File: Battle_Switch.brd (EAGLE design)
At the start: 160 x 100 mm, 10 parts, among them IC1 ATTINY13A

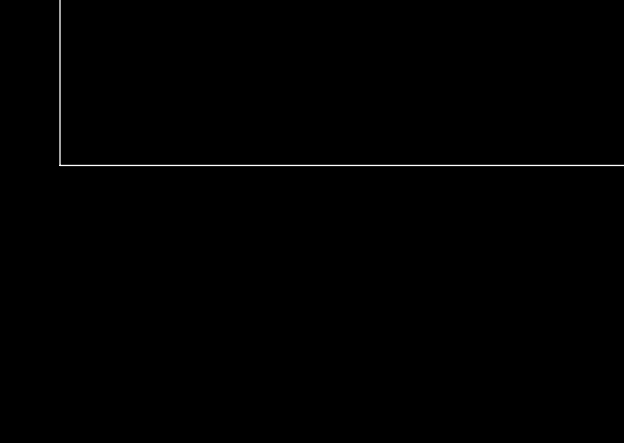
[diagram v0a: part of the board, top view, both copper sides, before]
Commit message: Added mode and threshold select jumpers.
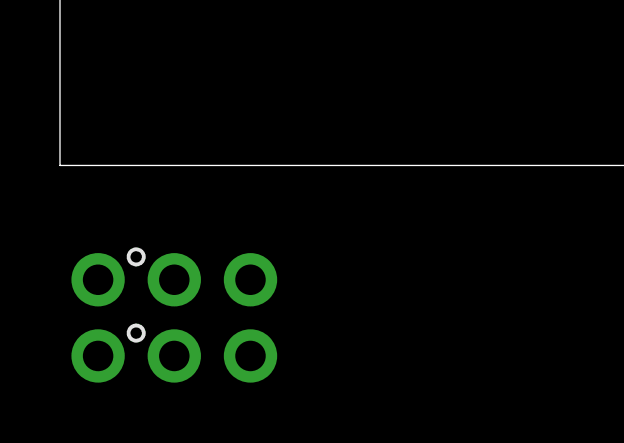
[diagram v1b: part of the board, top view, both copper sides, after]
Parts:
- added SJ1, SJ2: JUMPER-PTH-3-2OF3_NC, Battle_Switch:PTH-JUMPER-3-20F3_NC
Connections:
- new net THRESH_SEL: SJ2.P$1
- net GND: now also SJ1.P$2, SJ2.P$2
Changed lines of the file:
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@@
 <layer number="49" name="Reference" color="7" fill="1" visible="yes" active="yes"/>
 <layer number="50" name="dxf" color="7" fill="1" visible="no" active="no"/>
-<layer number="51" name="tDocu" color="7" fill="1" visible="no" active="yes"/>
+<layer number="51" name="tDocu" color="7" fill="1" visible="yes" active="yes"/>
 <layer number="52" name="bDocu" color="7" fill="1" visible="no" active="yes"/>
 <layer number="53" name="tGND_GNDA" color="7" fill="9" visible="no" active="no"/>
@@
 <element name="R1" library="Battle_Switch" package="0411/15" value="10k" x="25.4" y="60.96" rot="R180"/>
 <element name="R2" library="Battle_Switch" package="0411/15" value="10k" x="43.18" y="60.96" rot="R180"/>
+<element name="SJ2" library="Battle_Switch" package="PTH-JUMPER-3-20F3_NC" value="JUMPER-PTH-3-2OF3_NC" x="3.81" y="-3.81"/>
+<element name="SJ1" library="Battle_Switch" package="PTH-JUMPER-3-20F3_NC" value="JUMPER-PTH-3-2OF3_NC" x="3.81" y="-6.35"/>
 </elements>
 <signals>
@@
 <wire x1="54.61" y1="62.23" x2="54.61" y2="50.8" width="1.778" layer="16"/>
 <wire x1="41.91" y1="50.8" x2="54.61" y2="50.8" width="1.778" layer="16"/>
+<contactref element="SJ1" pad="P$2"/>
+<contactref element="SJ2" pad="P$2"/>
+<wire x1="3.81" y1="-3.81" x2="17.78" y2="60.96" width="0" layer="19" extent="1-1"/>
+<wire x1="3.81" y1="-6.35" x2="3.81" y2="-3.81" width="0" layer="19" extent="1-1"/>
 </signal>
 <signal name="VIN">
@@
 <contactref element="IC1" pad="P$7"/>
 </signal>
+<signal name="THRESH_SEL">
+<contactref element="SJ2" pad="P$1"/>
+</signal>
 </signals>

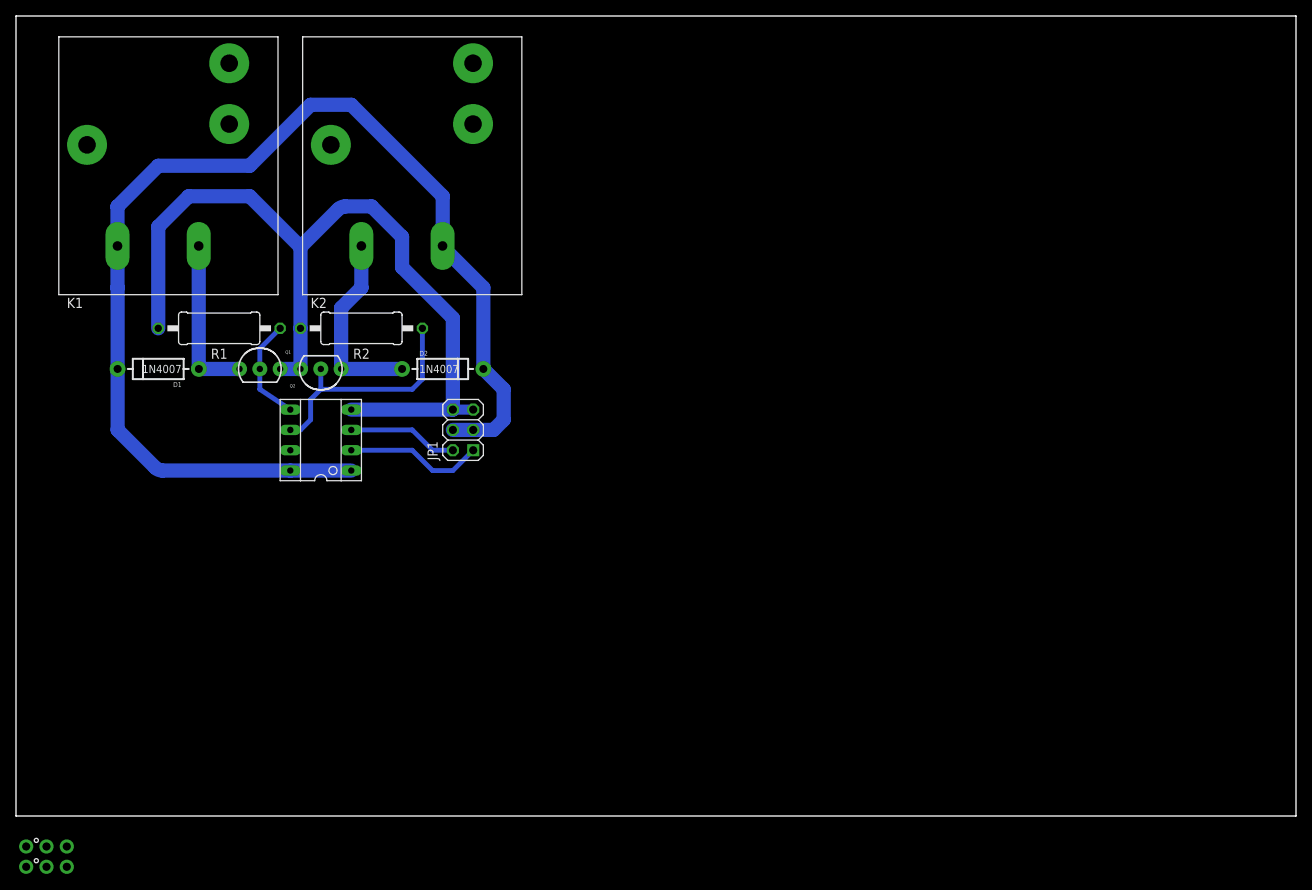
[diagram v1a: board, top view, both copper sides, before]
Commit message: Completed board layout.  Ready for copper ground pour.
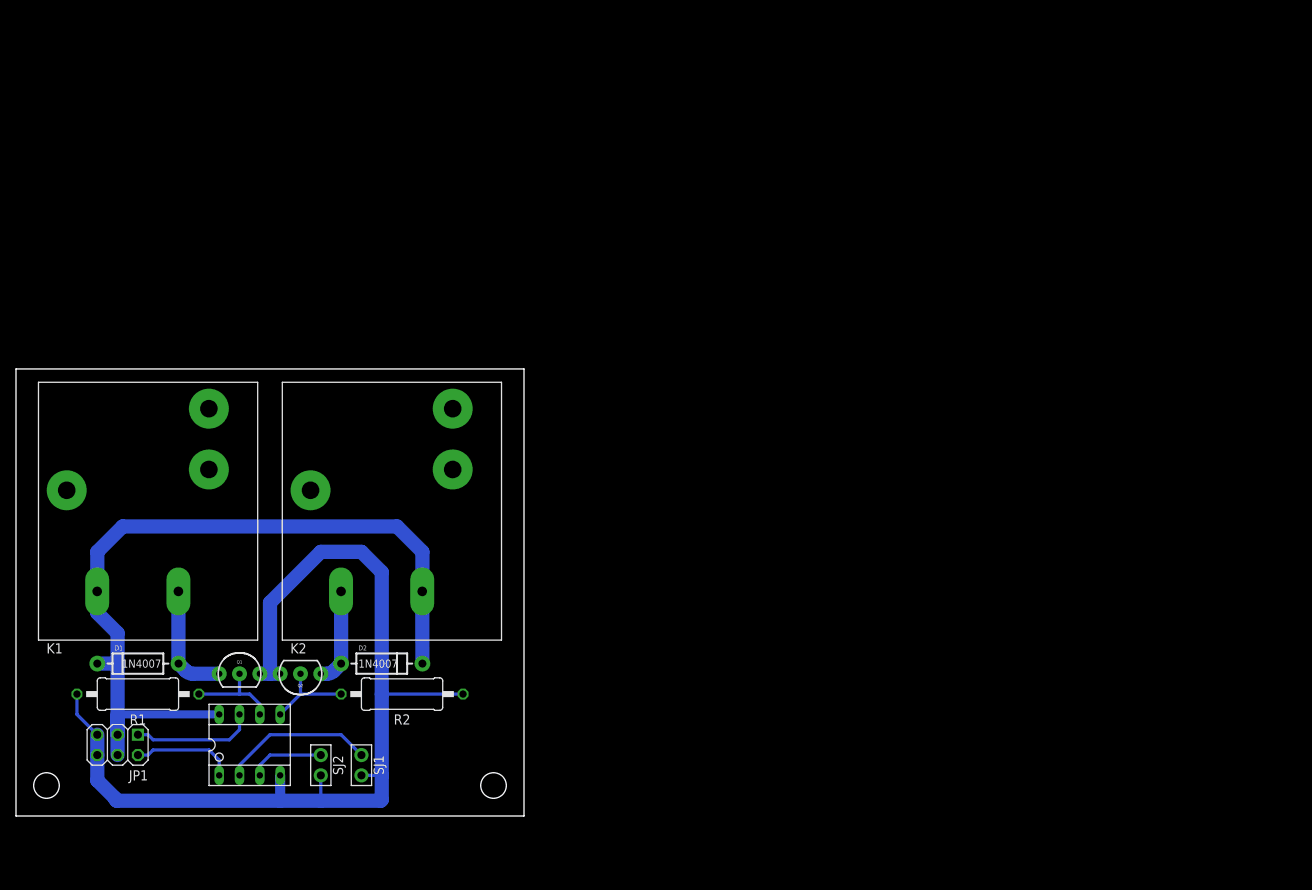
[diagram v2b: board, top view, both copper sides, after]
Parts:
- SJ1, SJ2: value JUMPER-PTH-3-2OF3_NC -> (none); device Battle_Switch:PTH-JUMPER-3-20F3_NC -> Battle_Switch:PTH-JUMPER-2-NO
- moved JP1 58.4 mm to (12.7, 8.89), turned to 180 degrees
- moved R1 46.8 mm to (15.2, 15.2)
- moved R2 46.0 mm to (48.3, 15.2)
- moved K1 43.3 mm to (16.5, 38.1)
- moved K2 43.3 mm to (47.0, 38.1)
- moved SJ1 41.4 mm to (43.2, 6.35), turned to 270 degrees
- moved IC1 39.1 mm to (29.2, 8.89), turned to 0 degrees
- moved Q1 38.2 mm to (27.9, 17.8)
- moved Q2 38.2 mm to (35.6, 17.8)
- moved D2 37.6 mm to (45.7, 19.1)
- moved D1 36.9 mm to (15.2, 19.1)
- moved SJ2 35.8 mm to (38.1, 6.35), turned to 270 degrees
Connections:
- removed net GND: IC1.P$4, JP1.5, JP1.6, Q1.1, Q2.1, R1.2, R2.2, SJ1.P$2, SJ2.P$2
- removed net VIN: D1.C, D2.C, IC1.P$1, IC1.P$8, JP1.3, JP1.4, K1.VC2, K2.VC1
- new net MODE_SEL: IC1.P$2, SJ1.P$1
- new net N$5: D1.C, D2.C, IC1.P$8, JP1.3, JP1.4, K1.VC2, K2.VC1
- net N$4: now also IC1.P$4, JP1.5, JP1.6, Q1.1, Q2.1, R1.2, R2.1, SJ1.P$2, SJ2.P$2; no longer IC1.P$7
- net OUT1: now also IC1.P$6; no longer IC1.P$5
- net OUT2: now also IC1.P$5, R2.2; no longer IC1.P$6, R2.1
- net SIG1: now also IC1.P$7; no longer IC1.P$2
- net SIG2: now also IC1.P$1; no longer IC1.P$3
- net THRESH_SEL: now also IC1.P$3
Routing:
- net VIN: track 152.7 -> 0.00 mm
- net N$4: track 0.00 -> 124.5 mm
- net GND: track 108.2 -> 0.00 mm
- net N$5: track 0.00 -> 101.8 mm
- net MODE_SEL: track 0.00 -> 19.1 mm
- net OUT2: track 29.5 -> 11.2 mm
- net N$3: track 24.0 -> 12.0 mm
- net THRESH_SEL: track 0.00 -> 9.42 mm
- net N$2: track 20.5 -> 14.6 mm
- net SIG1: track 17.3 -> 15.4 mm
- net OUT1: track 13.3 -> 12.0 mm
- net SIG2: track 13.8 -> 12.9 mm
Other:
- board size 160 x 100 mm -> 63.5 x 55.9 mm

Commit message: Revision A layout complete.  Ready for silkscreen additions.
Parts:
- removed JP1: (no value), Battle_Switch:2X03
- removed SJ2: (no value), Battle_Switch:PTH-JUMPER-2-NO
- added INPUT: (no value), Battle_Switch:2X03
- added THRESH_SEL: (no value), Battle_Switch:PTH-JUMPER-2-NO
- moved R2 1.52 mm to (46.7, 15.2)
- renumbered SJ1 to MODE_SEL
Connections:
- removed net N$4: IC1.P$4, JP1.5, JP1.6, MODE_SEL.P$2, Q1.1, Q2.1, R1.2, R2.1, SJ2.P$2
- removed net N$5: D1.C, D2.C, IC1.P$8, JP1.3, JP1.4, K1.VC2, K2.VC1
- new net GND: IC1.P$4, INPUT.5, INPUT.6, MODE_SEL.P$2, Q1.1, Q2.1, R1.2, R2.1, THRESH_SEL.P$2
- new net VIN: D1.C, D2.C, IC1.P$8, INPUT.3, INPUT.4, K1.VC2, K2.VC1
- net SIG1: now also INPUT.1; no longer JP1.1
- net SIG2: now also INPUT.2; no longer JP1.2
- net THRESH_SEL: now also THRESH_SEL.P$1; no longer SJ2.P$1
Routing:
- net N$4: track 124.5 -> 0.00 mm
- net VIN: track 0.00 -> 104.1 mm
- net N$5: track 101.8 -> 0.00 mm
- net GND: track 0.00 -> 16.4 mm
- net SIG2: track 12.9 -> 7.62 mm
- net SIG1: track 15.4 -> 13.8 mm
- net OUT2: track 11.2 -> 9.69 mm
- net MODE_SEL: track 19.1 -> 18.1 mm
- net THRESH_SEL: track 9.42 -> 10.4 mm
- net OUT1: track 12.0 -> 11.3 mm
- added copper zone on layer 16, net GND
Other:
- board text added: "1"
- board text added: "2"
